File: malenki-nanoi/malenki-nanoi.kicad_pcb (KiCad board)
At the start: 4 copper layers, 17.5 x 34 mm, 45 parts, among them J1 Conn_01x02_Male, J2 Conn_01x03, J3 Conn_01x02, J5 Conn_01x02_Male, J6 Conn_01x02_Male, J7 Conn_01x02_Male, U1 A7105, U2 AIC1734-33GUTR, U3 ATtiny1617-M, U5 DRV8837DSGR, U6 DRV8837DSGR, U7 DRV8837DSGR, Y1 16 Mhz 20ppm

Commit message: Another crazy version of rx
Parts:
- moved C22 0.09 mm to (95.4, 62.5)
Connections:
- U2 pad 1: Net-(U2-Pad1) -> GND
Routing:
- net GND: vias 14 -> 20

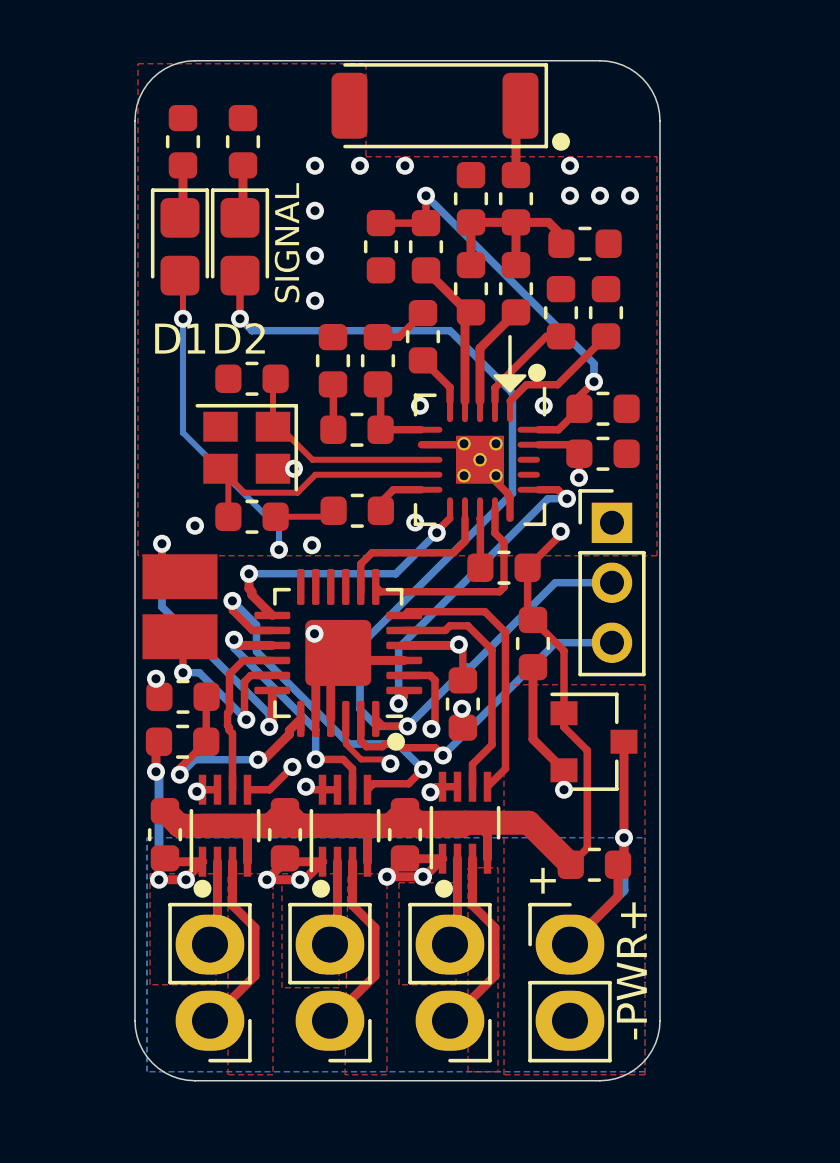
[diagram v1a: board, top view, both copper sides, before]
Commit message: A version of Malenki-nano with radio included on board
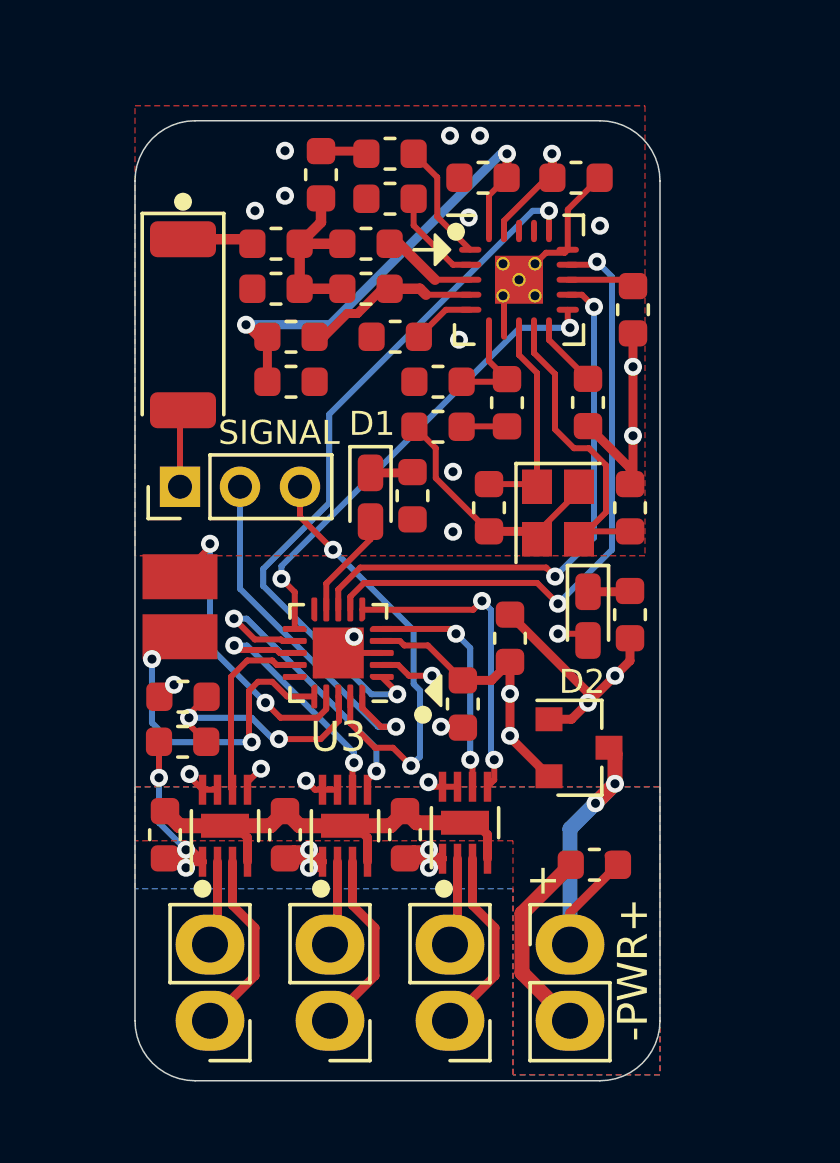
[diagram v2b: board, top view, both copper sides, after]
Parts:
- D1, D2: footprint LED_SMD:LED_0805_2012Metric_Castellated -> LED_SMD:LED_0603_1608Metric_Castellated
- R1, R2: value 220R -> 100R
- U3: value ATtiny1617-M -> ATtiny1616-M; footprint malenki-nano:qfn24-hand1 -> Package_DFN_QFN:VQFN-20-1EP_3x3mm_P0.4mm_EP1.7x1.7mm
- moved R2 20.4 mm to (104.5, 66.0), turned to -90 degrees
- moved D2 16.9 mm to (103.1, 66.0)
- moved J2 14.4 mm to (89.5, 61.7), turned to 90 degrees
- moved R1 14.1 mm to (97.2, 62.0), turned to -90 degrees
- moved C14 12.6 mm to (104.5, 62.4), turned to 90 degrees
- moved AE1 11.1 mm to (89.6, 56.3), turned to -90 degrees
- moved Y1 10.6 mm to (102.1, 62.6), turned to -90 degrees
- moved D1 10.5 mm to (95.8, 62.0)
- moved C23 9.62 mm to (104.6, 55.8), turned to -90 degrees
- moved C21 9.24 mm to (102.7, 51.4)
- moved C9 9.10 mm to (94.2, 51.3), turned to 90 degrees
- moved C15 8.99 mm to (99.8, 62.4), turned to -90 degrees
- moved C16 8.94 mm to (96.5, 50.6), turned to 180 degrees
- moved C20 8.68 mm to (99.6, 51.4), turned to 180 degrees
- moved C22 8.50 mm to (103.1, 58.9), turned to -90 degrees
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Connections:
- U3 pad 11: Net-(U3-Pad11) -> SPI_SCS
- U3 pad 12: Net-(U3-Pad12) -> MOTOR2F
- U3 pad 13: SPI_SCS -> MOTOR2R
- U3 pad 14: MOTOR2F -> MOTOR1R
- U3 pad 15: MOTOR2R -> Net-(U3-Pad15)
- U3 pad 16: MOTOR1R -> WEAPON2
- U3 pad 17: WEAPON2 -> WEAPON3
- U3 pad 18: WEAPON3 -> VSENSE
- U3 pad 19: VSENSE -> UPDI
- U3 pad 20: GND -> TXDEBUG
- U3 pad 9: Net-(U3-Pad9) -> BLINKY
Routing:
- net BLINKY: track 21.6 -> 3.75 mm, vias 3 -> 0
- net TXDEBUG: track 36.0 -> 20.1 mm
- net SPI_SDIO: track 7.15 -> 21.2 mm, vias 0 -> 2
- net SPI_SCK: track 5.53 -> 18.9 mm, vias 0 -> 2
- net GIO1: track 11.1 -> 24.3 mm
- net SPI_SCS: track 9.21 -> 15.8 mm
- net GND: track 56.2 -> 61.0 mm, vias 20 -> 17
- net WEAPON2: track 6.52 -> 11.2 mm
- net UPDI: track 10.9 -> 14.6 mm, vias 1 -> 2
- net VLOGIC: track 12.7 -> 16.2 mm
- net MOTOR2F: track 13.2 -> 10.4 mm
- net /radio/REGOA: track 13.7 -> 16.3 mm
- net VBAT: track 29.5 -> 27.4 mm, vias 8 -> 9
- net Net-(C14-Pad1): track 8.99 -> 10.5 mm
- net MOTOR3F: track 9.11 -> 10.6 mm, vias 0 -> 2
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- removed copper zone on F.Cu, net Net-(J5-Pad1)
- removed copper zone on F.Cu, net Net-(J5-Pad2)
- removed copper zone on F.Cu, net Net-(J6-Pad1)
- removed copper zone on F.Cu, net Net-(J6-Pad2)
- removed copper zone on F.Cu, net Net-(J7-Pad1)
- removed copper zone on F.Cu, net Net-(J7-Pad2)
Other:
- board size 17.5 x 34 mm -> 17.5 x 32 mm
- net class Default: clearance 0.2 -> 0.15
- rule trace_clearance: 0.2 -> 0.15

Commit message: 4-layer Malenki-nano
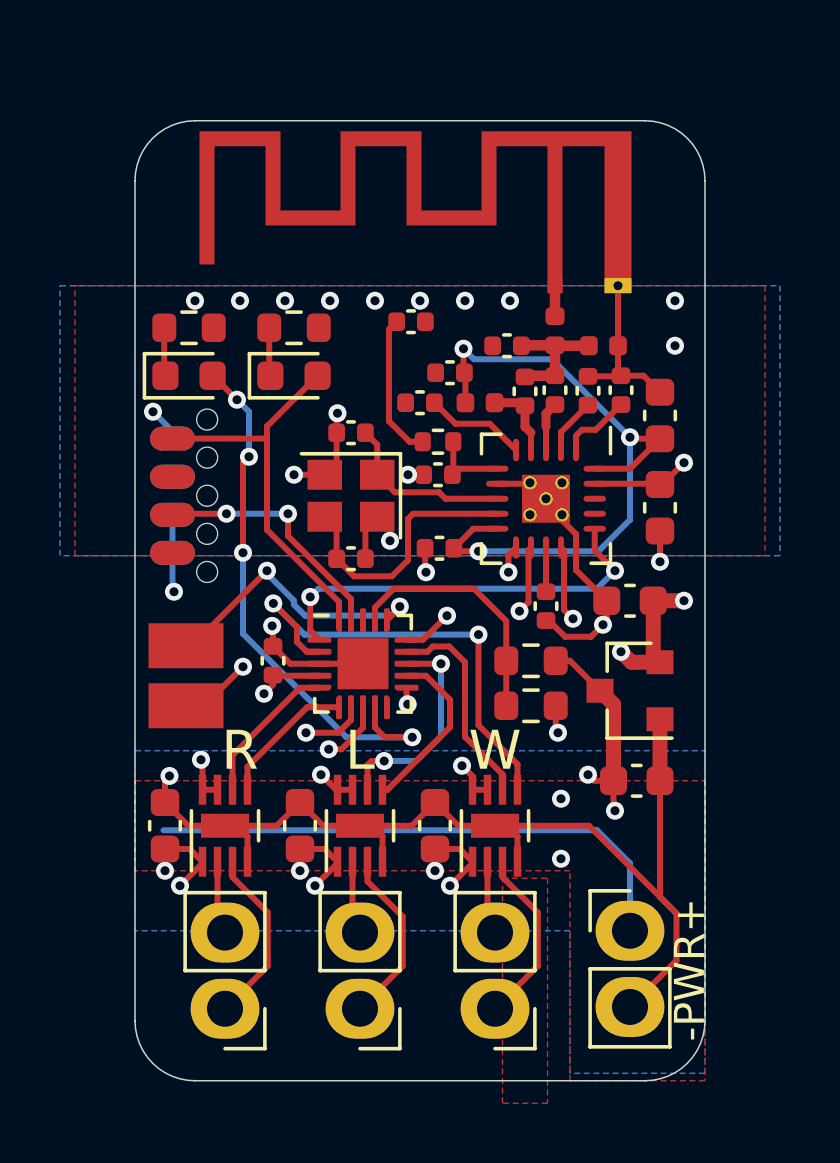
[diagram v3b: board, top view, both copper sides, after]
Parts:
- removed C7: 10uF, Capacitor_SMD:C_0603_1608Metric
- removed J7: Conn_01x02_Male, malenki-nano:PinHeader_1x02_P2.54mm_BIG1
- removed U7: DRV8837DSGR, malenki-nano:WSON-8-1EP_2x2mm_P0.5mm_HAND1
- added C1: 10uF, Capacitor_SMD:C_0603_1608Metric, F.Cu at (98.0, 73.0)
- added J4: Conn_01x02_Male-Connector, malenki-nano:PinHeader_1x02_P2.54mm_BIG1, F.Cu at (100.0, 79.1)
- added U4: DRV8837DSGR, malenki-nano:WSON-8-1EP_2x2mm_P0.5mm_HAND1, F.Cu at (100.0, 73.0)
- AE1: value Rainsun AN2051-245 -> ~; footprint RF_Antenna:Johanson_2450AT43F0100 -> RF_Antenna:Texas_SWRA117D_2.4GHz_Left
- C10, C11, C12, C13, C14, C15, C16, C17, C18, C19, C22, C23, C9: footprint Capacitor_SMD:C_0603_1608Metric -> Capacitor_SMD:C_0402_1005Metric
- C4: value 0.1uF -> 100nF; footprint Capacitor_SMD:C_0603_1608Metric -> Capacitor_SMD:C_0402_1005Metric
- D1, D2: footprint LED_SMD:LED_0603_1608Metric_Castellated -> LED_SMD:LED_0603_1608Metric
- J1, J5, J6: value Conn_01x02_Male -> Conn_01x02_Male-Connector
- J2: value Conn_01x03 -> Conn_01x08_Male; footprint Connector_PinHeader_2.00mm:PinHeader_1x03_P2.00mm_Vertical -> malenki-nano:SOIC_clipProgSmall; moved to B.Cu
- L1, L2, L3: footprint Inductor_SMD:L_0603_1608Metric -> Inductor_SMD:L_0402_1005Metric
- R5: value 200 -> 200R; footprint Resistor_SMD:R_0603_1608Metric -> Resistor_SMD:R_0402_1005Metric
- moved R2 14.7 mm to (93.3, 56.4), turned to 0 degrees
- moved D2 12.7 mm to (93.3, 58.0), turned to 0 degrees
- moved AE1 12.5 mm to (102.0, 55.0), turned to 0 degrees
- moved R3 11.9 mm to (101.2, 67.5), turned to 180 degrees
- moved R4 11.6 mm to (101.2, 69.0), turned to 0 degrees
- moved C21 11.4 mm to (105.5, 62.4), turned to -90 degrees
- moved L2 11.1 mm to (103.6, 57.0), turned to 0 degrees
- moved C16 11.0 mm to (104.2, 58.5), turned to 90 degrees
- moved C23 10.3 mm to (101.7, 65.7)
- moved C20 9.88 mm to (105.5, 59.3), turned to 90 degrees
- moved L1 9.74 mm to (102.0, 56.5), turned to -90 degrees
- moved C14 9.46 mm to (95.2, 64.1), turned to 0 degrees
- moved R1 9.32 mm to (89.8, 56.4), turned to 0 degrees
- moved C17 9.19 mm to (103.1, 58.5), turned to 90 degrees
- moved C9 8.42 mm to (100.4, 57.0), turned to 180 degrees
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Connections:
- net Net-(U1-Pad17) renamed no_connect_44
- net Net-(U1-Pad18) renamed no_connect_45
- net Net-(U3-Pad10) renamed no_connect_46
- C22 pad 1: Net-(C22-Pad1) -> /radio/REGOA
- J2 pad 1: GND -> VBAT
- J2 pad 2: TXDEBUG -> no_connect_41
- J2 pad 3: UPDI -> GND
- U1 pad 10: Net-(C22-Pad1) -> /radio/REGOA
- U3 pad 15: Net-(U3-Pad15) -> WEAPON2
- U3 pad 16: WEAPON2 -> WEAPON3
- U3 pad 17: WEAPON3 -> VSENSE
- U3 pad 18: VSENSE -> no_connect_47
- U5 pad 5: MOTOR1F -> MOTOR2F
- U5 pad 6: MOTOR1R -> MOTOR2R
- U6 pad 5: MOTOR2F -> MOTOR3F
- U6 pad 6: MOTOR2R -> MOTOR3R
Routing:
- net VBAT: track 27.4 -> 51.7 mm
- net BLINKY: track 3.75 -> 18.3 mm, vias 0 -> 4
- net GIO1: track 24.3 -> 13.8 mm
- net SPI_SCS: track 15.8 -> 8.28 mm
- net /radio/REGOA: track 16.3 -> 23.0 mm, vias 2 -> 3
- net TXDEBUG: track 20.1 -> 13.4 mm, vias 2 -> 0
- net Net-(J7-Pad1): track 6.33 -> 0.00 mm
- net UPDI: track 14.6 -> 8.28 mm
- net Net-(J4-Pad1): track 0.00 -> 5.98 mm
- net MOTOR3F: track 10.6 -> 4.64 mm, vias 2 -> 0
- net MOTOR1F: track 9.69 -> 15.5 mm
- net GND: track 61.0 -> 65.8 mm, vias 17 -> 23
- net MOTOR2F: track 10.4 -> 5.81 mm, vias 2 -> 0
- net SPI_SDIO: track 21.2 -> 17.0 mm
- net SPI_SCK: track 18.9 -> 15.0 mm
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- added copper zone on B.Cu, net GND
- added copper zone on F.Cu, net Net-(J4-Pad1)
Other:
- board size 17.5 x 32 mm -> 19 x 32 mm
- net class Default removed
- net class rf removed
- board text added: "L"
- board text added: "R"
- board text added: "W"
- board text removed: "+"
- board text removed: "SIGNAL"

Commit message: Zones, footprints etc
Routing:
- added copper zone on F.Cu, net Net-(J4-Pad2)
- added copper zone on F.Cu, net Net-(J5-Pad1)
- added copper zone on F.Cu, net Net-(J5-Pad2)
- added copper zone on F.Cu, net Net-(J6-Pad1)
- added copper zone on F.Cu, net Net-(J6-Pad2)
